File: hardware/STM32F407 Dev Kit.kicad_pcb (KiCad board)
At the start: 2 copper layers, 65.2 x 58.4 mm, 153 parts, among them J1 GMSB0531112YEU, J10 Conn_01x04, J11 TBC 2.54mm 10A, J12 IMP34DT05, J2 Conn_01x06, J3 RJMG1S8008101BR, J4 B2B-XH-A(LF)(SN), J5 Conn_01x04, J7 SJ-3524-SMT, J8 GMSB0531112YEU, J9 Conn_01x04, SW1 SW TACT-SPST, SW2 SW TACT-SPST, SW3 SW TACT-SPST, U1 STM32F103CBT6, U2 DP83826IRHBR, U3 DRV8701ERGET, U4 DMHT6016LFJ-13, U5 ADS122C04IPW, U6 CS43L22, U7 STM32F407VGT6, U8 AP63203WU, U9 XC6206P182MR, Y1 ABM8G-8.000MHZ-18-D2Y-T, Y2 ABM8G-25.000MHZ-9-B4Y-T, Y3 ABM8G-8.000MHZ-18-D2Y-T

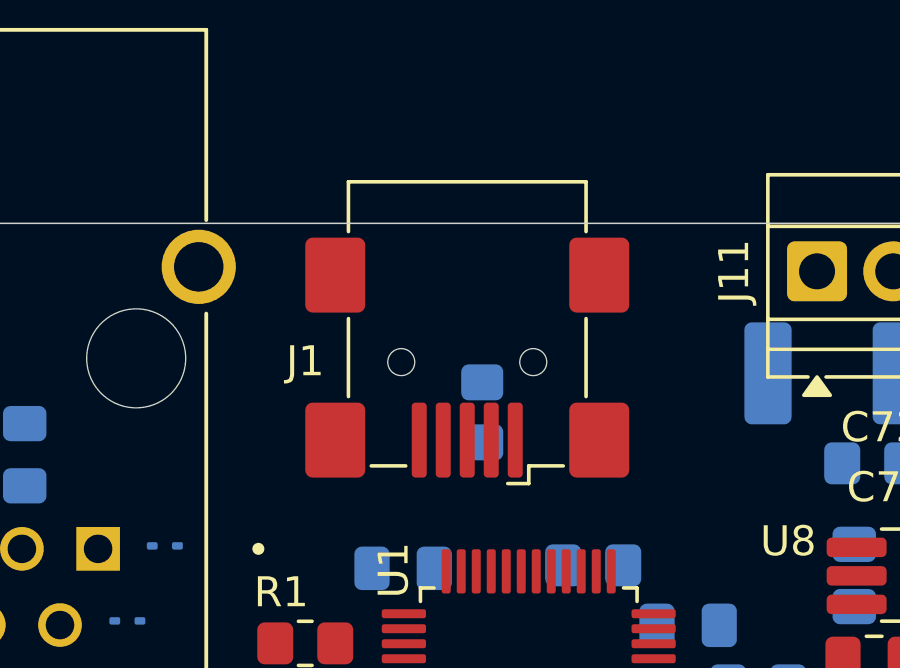
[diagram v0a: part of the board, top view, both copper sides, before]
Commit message: Review Component Placement
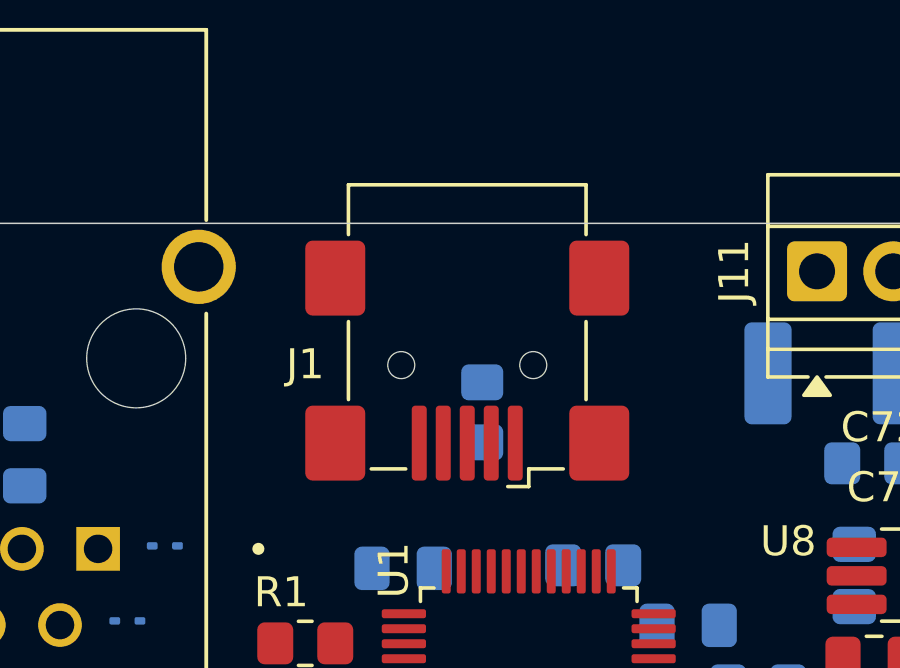
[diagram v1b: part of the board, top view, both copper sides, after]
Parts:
- moved J1 0.10 mm to (184.0, 54.7)

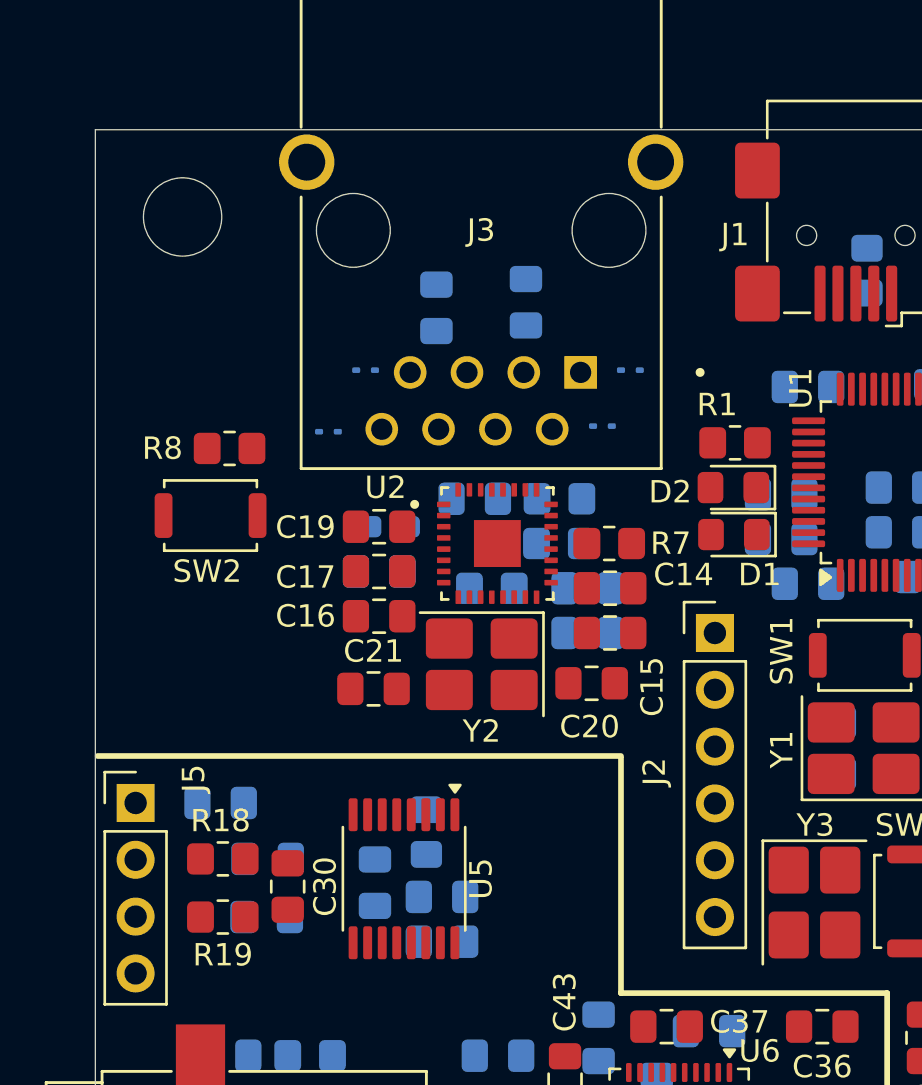
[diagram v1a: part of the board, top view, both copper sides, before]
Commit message: Route Ethernet section and add global labels
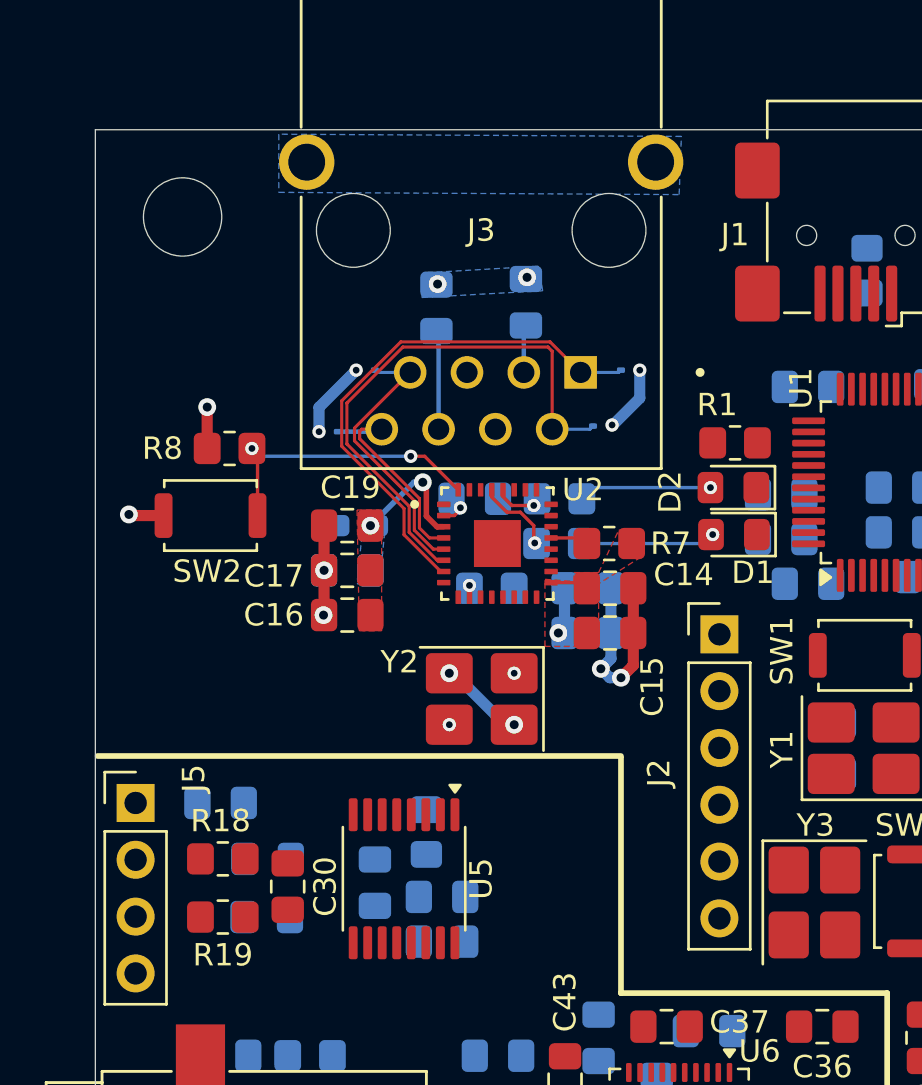
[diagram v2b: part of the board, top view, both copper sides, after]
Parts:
- C20, C21: moved to B.Cu
- moved C21 5.04 mm to (167.2, 76.5), turned to 180 degrees
- moved C20 4.93 mm to (167.3, 74.5), turned to 0 degrees
- moved Y2 1.55 mm to (167.3, 75.5)
- moved C16 1.43 mm to (161.3, 71.7)
- moved C17 1.43 mm to (161.3, 69.7)
- moved C18 1.43 mm to (161.3, 69.7)
- moved C19 1.43 mm to (161.3, 67.7)
- moved FB1 1.43 mm to (161.7, 67.7)
- moved J2 0.21 mm to (177.9, 72.6)
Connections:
- net /[5] - Motor Driver/nSLEEP renamed nSLEEP
- net /[7] - DAC & Mic/MIC_DOUT renamed MIC_DOUT
- C57 pad 1: /[8] - STM32F407/F407_NTRST -> F407_NTRST
- C83 pad 1: /[9] - Power/SHEILD -> SHEILD
- J11 pad 2: /[9] - Power/SHEILD -> SHEILD
- J12 pad 3: /[7] - DAC & Mic/MIC_CLK -> MIC_CLK
- J3 pad S1: /[4] - Ethernet PHY/SHEILD -> SHEILD
- J3 pad S2: /[4] - Ethernet PHY/SHEILD -> SHEILD
- R10 pad 1: /[5] - Motor Driver/EN -> EN
- R14 pad 2: /[5] - Motor Driver/nFAULT -> nFAULT
- R15 pad 2: /[5] - Motor Driver/SNSOUT -> SNSOUT
- R17 pad 2: /[6] - ADC/ADC_RST -> ADC_RST
- R2 pad 2: /[3] - STM32F103 debugger/F407_JTMS -> F407_JTMS
- R20 pad 2: /[7] - DAC & Mic/CS43L22_RST -> CS43L22_RST
- R26 pad 1: /[9] - Power/SHEILD -> SHEILD
- R5 pad 1: /[4] - Ethernet PHY/CRS -> CRS
- R6 pad 1: /[4] - Ethernet PHY/COL -> COL
- R8 pad 2: /[4] - Ethernet PHY/PHY_NRST -> PHY_NRST
- SW2 pad 2: /[4] - Ethernet PHY/PHY_NRST -> PHY_NRST
- SW3 pad 2: /[8] - STM32F407/F407_NTRST -> F407_NTRST
- U1 pad 18: /[3] - STM32F103 debugger/F407_NTRST -> F407_NTRST
- U1 pad 26: /[3] - STM32F103 debugger/F407_JTCLK -> F407_JTCLK
- U1 pad 27: /[3] - STM32F103 debugger/F407_JTMS -> F407_JTMS
- U2 pad 11: /[4] - Ethernet PHY/MDIO -> MDIO
- U2 pad 12: /[4] - Ethernet PHY/MDC -> MDC
- U2 pad 13: /[4] - Ethernet PHY/RX_D3 -> RX_D3
- U2 pad 14: /[4] - Ethernet PHY/RX_D2 -> RX_D2
- U2 pad 15: /[4] - Ethernet PHY/RX_D1 -> RX_D1
- U2 pad 16: /[4] - Ethernet PHY/RX_D0 -> RX_D0
- U2 pad 18: /[4] - Ethernet PHY/RX_DV -> RX_DV
- U2 pad 19: /[4] - Ethernet PHY/RX_CLK -> RX_CLK
- U2 pad 20: /[4] - Ethernet PHY/RX_ER -> RX_ER
- U2 pad 22: /[4] - Ethernet PHY/TX_CLK -> TX_CLK
- U2 pad 23: /[4] - Ethernet PHY/TX_EN -> TX_EN
- U2 pad 24: /[4] - Ethernet PHY/TX_D0 -> TX_D0
- U2 pad 25: /[4] - Ethernet PHY/TX_D1 -> TX_D1
- U2 pad 26: /[4] - Ethernet PHY/TX_D2 -> TX_D2
- U2 pad 27: /[4] - Ethernet PHY/TX_D3 -> TX_D3
- U2 pad 28: /[4] - Ethernet PHY/COL -> COL
- U2 pad 29: /[4] - Ethernet PHY/CRS -> CRS
- U2 pad 32: /[4] - Ethernet PHY/PHY_NRST -> PHY_NRST
- U3 pad 10: /[5] - Motor Driver/SNSOUT -> SNSOUT
- U3 pad 11: /[5] - Motor Driver/SO -> SO
- U3 pad 14: /[5] - Motor Driver/EN -> EN
- U3 pad 15: /[5] - Motor Driver/PH -> PH
- U3 pad 9: /[5] - Motor Driver/nFAULT -> nFAULT
- U5 pad 14: /[6] - ADC/ADC_DRDY -> ADC_DRDY
- U5 pad 15: /[6] - ADC/SDA -> SDA
- U5 pad 16: /[6] - ADC/SCL -> SCL
- U5 pad 3: /[6] - ADC/ADC_RST -> ADC_RST
- U6 pad 1: /[7] - DAC & Mic/SDA -> SDA
- U6 pad 2: /[7] - DAC & Mic/SCL -> SCL
- U6 pad 32: /[7] - DAC & Mic/CS43L22_RST -> CS43L22_RST
- U6 pad 37: /[7] - DAC & Mic/CS43L22_MCLK -> CS43L22_MCLK
- U6 pad 38: /[7] - DAC & Mic/CS43L22_SCLK -> CS43L22_SCLK
- U6 pad 39: /[7] - DAC & Mic/CS43L22_SDIN -> CS43L22_SDIN
- U6 pad 40: /[7] - DAC & Mic/CS43L22_LRCK -> CS43L22_LRCK
- U7 pad 14: /[8] - STM32F407/F407_NTRST -> F407_NTRST
- U7 pad 16: /[8] - STM32F407/MDC -> MDC
- U7 pad 17: /[8] - STM32F407/TX_D2 -> TX_D2
- U7 pad 18: /[8] - STM32F407/TX_CLK -> TX_CLK
- U7 pad 23: /[8] - STM32F407/CRS -> CRS
- U7 pad 24: /[8] - STM32F407/RX_CLK -> RX_CLK
- U7 pad 25: /[8] - STM32F407/MDIO -> MDIO
- U7 pad 26: /[8] - STM32F407/COL -> COL
- U7 pad 29: /[8] - STM32F407/CS43L22_MCLK -> CS43L22_MCLK
- U7 pad 30: /[8] - STM32F407/SO -> SO
- U7 pad 32: /[8] - STM32F407/RX_DV -> RX_DV
- U7 pad 33: /[8] - STM32F407/RX_D0 -> RX_D0
- U7 pad 34: /[8] - STM32F407/RX_D1 -> RX_D1
- U7 pad 35: /[8] - STM32F407/RX_D2 -> RX_D2
- U7 pad 36: /[8] - STM32F407/RX_D3 -> RX_D3
- U7 pad 45: /[8] - STM32F407/EN -> EN
- U7 pad 47: /[8] - STM32F407/RX_ER -> RX_ER
- U7 pad 48: /[8] - STM32F407/TX_EN -> TX_EN
- U7 pad 51: /[8] - STM32F407/TX_D0 -> TX_D0
- U7 pad 52: /[8] - STM32F407/TX_D1 -> TX_D1
- U7 pad 54: /[8] - STM32F407/CS43L22_RST -> CS43L22_RST
- U7 pad 55: /[8] - STM32F407/ADC_RST -> ADC_RST
- U7 pad 56: /[8] - STM32F407/ADC_DRDY -> ADC_DRDY
- U7 pad 61: /[8] - STM32F407/SNSOUT -> SNSOUT
- U7 pad 62: /[8] - STM32F407/nFAULT -> nFAULT
- U7 pad 63: /[8] - STM32F407/PH -> PH
- U7 pad 64: /[8] - STM32F407/PHY_NRST -> PHY_NRST
- U7 pad 65: /[8] - STM32F407/MIC_CLK -> MIC_CLK
- U7 pad 72: /[8] - STM32F407/F407_JTMS -> F407_JTMS
- U7 pad 76: /[8] - STM32F407/F407_JTCLK -> F407_JTCLK
- U7 pad 80: /[8] - STM32F407/CS43L22_SDIN -> CS43L22_SDIN
- U7 pad 89: /[8] - STM32F407/CS43L22_SCLK -> CS43L22_SCLK
- U7 pad 90: /[8] - STM32F407/CS43L22_LRCK -> CS43L22_LRCK
- U7 pad 95: /[8] - STM32F407/TX_D3 -> TX_D3
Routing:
- net GND: track 0.00 -> 25.2 mm, vias 0 -> 13
- net /[4] - Ethernet PHY/TD_N: track 0.00 -> 24.7 mm
- net /[4] - Ethernet PHY/TD_P: track 0.00 -> 23.8 mm
- net PHY_NRST: track 0.00 -> 13.1 mm, vias 0 -> 2
- net /[4] - Ethernet PHY/RD_P: track 0.00 -> 12.5 mm
- net /[4] - Ethernet PHY/RD_N: track 0.00 -> 10.3 mm
- net Net-(U2-VDDA3V3): track 0.00 -> 6.40 mm, vias 0 -> 2
- net Net-(D1-A): track 0.00 -> 6.12 mm, vias 0 -> 1
- net +3V3: track 0.00 -> 6.00 mm, vias 0 -> 2
- net Net-(D2-A): track 0.00 -> 5.96 mm, vias 0 -> 1
- net /[4] - Ethernet PHY/TCT2: track 0.00 -> 4.43 mm
- net CRS: track 0.00 -> 3.52 mm, vias 0 -> 1
- net COL: track 0.00 -> 2.20 mm, vias 0 -> 1
- net /[4] - Ethernet PHY/TCT1: track 0.00 -> 2.14 mm
- net /[4] - Ethernet PHY/INT: track 0.00 -> 1.70 mm
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- added copper zone on F.Cu, net +3V3
- added copper zone on In2.Cu, net +3V3
- added copper zone on B.Cu, net GND
- added copper zone on In1.Cu, net GND
- added copper zone on B.Cu, net Net-(U2-VDDA3V3)
- added copper zone on F.Cu, net Net-(U2-VDDA3V3)
- added copper zone on B.Cu, net SHEILD
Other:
- copper layers 2 -> 4

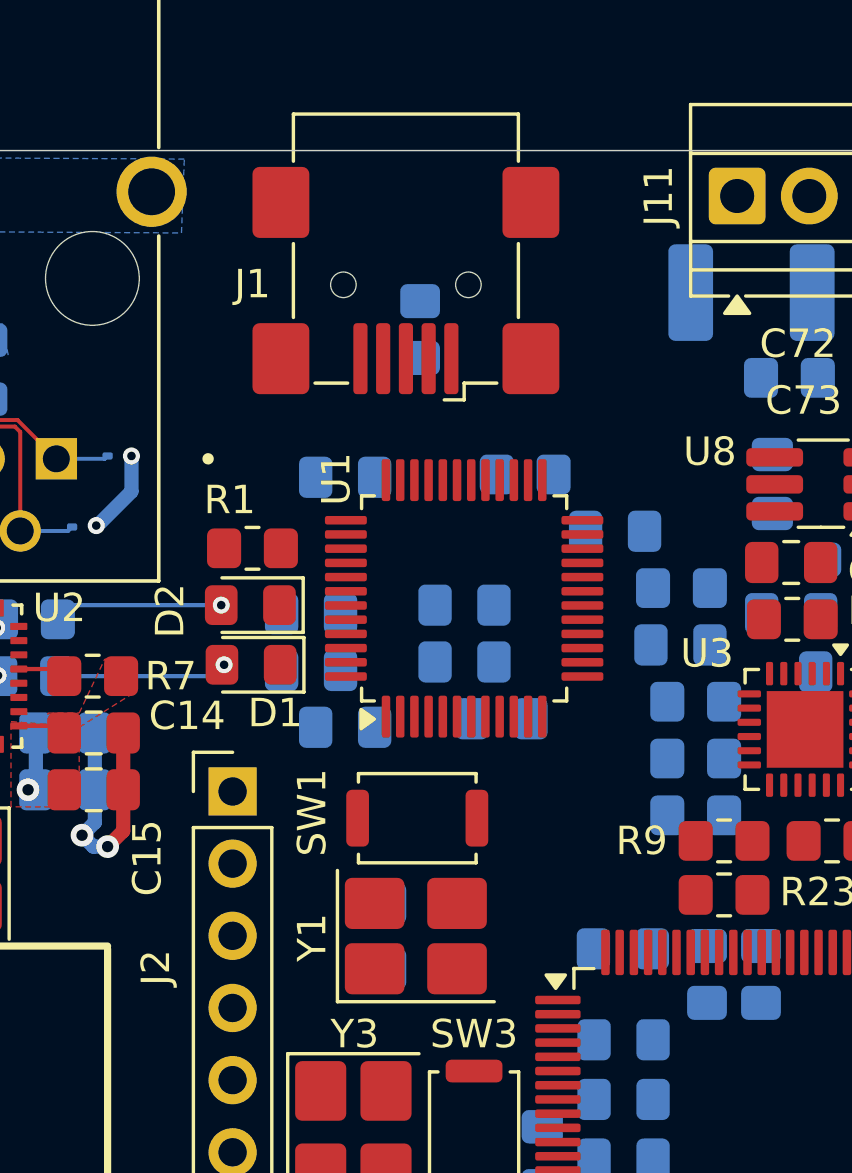
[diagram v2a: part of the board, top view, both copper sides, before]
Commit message: Route STM32F103 debugger section
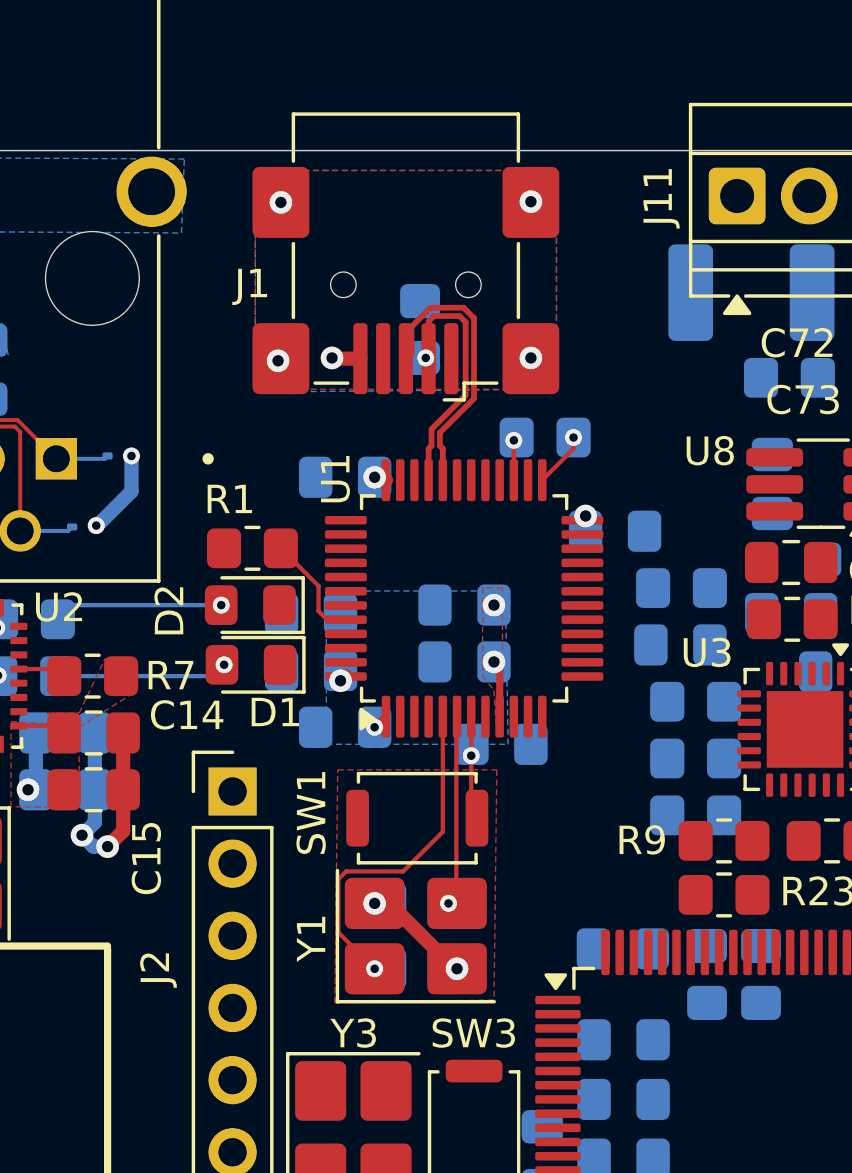
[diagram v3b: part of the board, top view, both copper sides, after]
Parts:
- moved R2 1.48 mm to (188.9, 60.1)
- moved C1 0.90 mm to (187.4, 70.9)
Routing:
- net /[3] - STM32F103 debugger/F103_OSC_IN: track 0.00 -> 12.6 mm, vias 0 -> 1
- net /[3] - STM32F103 debugger/F103_USB_N: track 0.00 -> 10.1 mm
- net /[3] - STM32F103 debugger/F103_USB_P: track 0.00 -> 8.99 mm, vias 0 -> 1
- net /[3] - STM32F103 debugger/F103_OSC_OUT: track 0.00 -> 6.90 mm, vias 0 -> 1
- net GND: track 25.2 -> 31.1 mm, vias 13 -> 20
- net /[3] - STM32F103 debugger/F103_NRST: track 0.00 -> 4.97 mm, vias 0 -> 1
- net +3V3: track 6.00 -> 9.99 mm, vias 2 -> 8
- net /[3] - STM32F103 debugger/F103_BOOT0: track 0.00 -> 3.85 mm
- net Net-(U1-PB12): track 0.00 -> 1.96 mm, vias 0 -> 1
- net F407_JTMS: track 0.00 -> 1.54 mm, vias 0 -> 1
- added copper zone on B.Cu, net +3V3
- added copper zone on F.Cu, net GND

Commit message: Route power section
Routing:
- net /[3] - STM32F103 debugger/F103_JTDO: track 0.00 -> 26.0 mm
- net GND: track 31.1 -> 55.8 mm, vias 20 -> 50
- net /[3] - STM32F103 debugger/F103_JTCK: track 0.00 -> 22.2 mm, vias 0 -> 1
- net +3V3: track 9.99 -> 31.9 mm, vias 8 -> 9
- net /[3] - STM32F103 debugger/F103_JTMS: track 0.00 -> 21.6 mm, vias 0 -> 1
- net +12V: track 0.00 -> 17.4 mm, vias 0 -> 5
- net /[3] - STM32F103 debugger/F103_JTDI: track 0.00 -> 14.4 mm
- net /[3] - STM32F103 debugger/F103_NJRST: track 0.00 -> 13.6 mm
- added copper zone on F.Cu, net +12V
- added copper zone on In2.Cu, net +12V

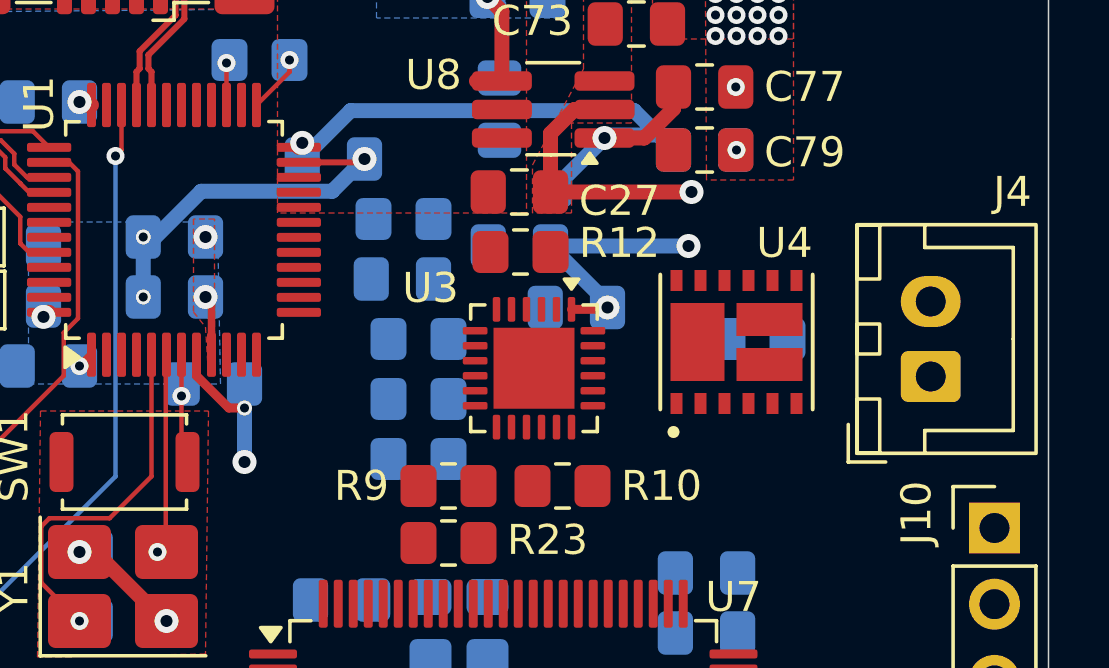
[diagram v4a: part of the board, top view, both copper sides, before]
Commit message: Route Motor Driver section
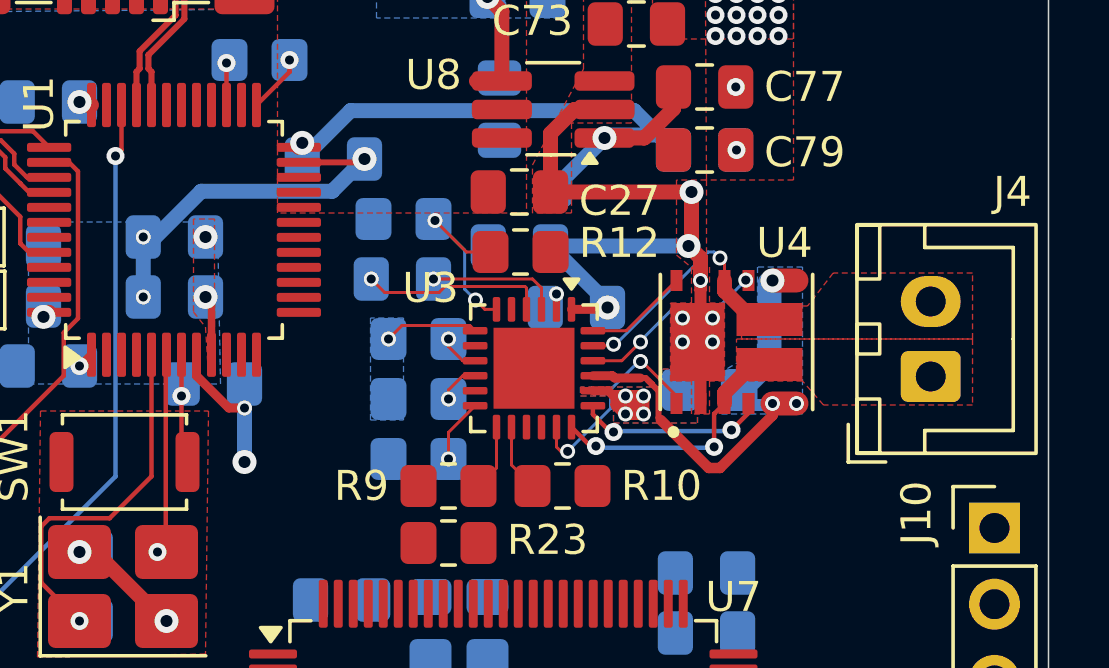
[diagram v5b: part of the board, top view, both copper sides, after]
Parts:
- moved R16 2.33 mm to (203.9, 71.1)
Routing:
- net /[5] - Motor Driver/SP: track 0.00 -> 17.0 mm, vias 0 -> 3
- net +12V: track 17.4 -> 27.5 mm, vias 5 -> 10
- net /[5] - Motor Driver/SH1: track 0.00 -> 8.88 mm, vias 0 -> 2
- net /[5] - Motor Driver/SH2: track 0.00 -> 8.67 mm, vias 0 -> 2
- net /[5] - Motor Driver/GH1: track 0.00 -> 7.06 mm, vias 0 -> 2
- net /[5] - Motor Driver/VREF: track 0.00 -> 6.39 mm, vias 0 -> 2
- net /[5] - Motor Driver/GL2: track 0.00 -> 6.33 mm, vias 0 -> 2
- net /[5] - Motor Driver/GL1: track 0.00 -> 6.30 mm, vias 0 -> 2
- net /[5] - Motor Driver/CPL: track 0.00 -> 6.18 mm, vias 0 -> 1
- net GND: track 55.8 -> 61.8 mm, vias 50 -> 54
- net /[5] - Motor Driver/CPH: track 0.00 -> 4.44 mm, vias 0 -> 1
- net /[5] - Motor Driver/GH2: track 0.00 -> 3.48 mm
- net AVDD: track 0.00 -> 3.15 mm, vias 0 -> 1
- net EN: track 0.00 -> 2.25 mm
- net nSLEEP: track 0.00 -> 2.21 mm
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- added copper zone on F.Cu, net /[5] - Motor Driver/SH1
- added copper zone on F.Cu, net /[5] - Motor Driver/SH2
- added copper zone on B.Cu, net /[5] - Motor Driver/SP
- added copper zone on B.Cu, net AVDD
